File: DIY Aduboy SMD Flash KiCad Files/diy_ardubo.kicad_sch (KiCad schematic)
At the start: 21 parts, among them J1 Conn_02x01, J2 Conn_01x07_Pin, J3 Conn_02x03_Odd_Even, J4 Conn_01x01_Pin, Q1 BC557, SW1 SW_Push, SW2 SW_Push, SW3 SW_Push, SW4 SW_Push, SW5 SW_Push, SW6 SW_Push, SW7 SW_Push, SW8 SW_SPDT, U1 ProMicro, U2 W25Q128JVS

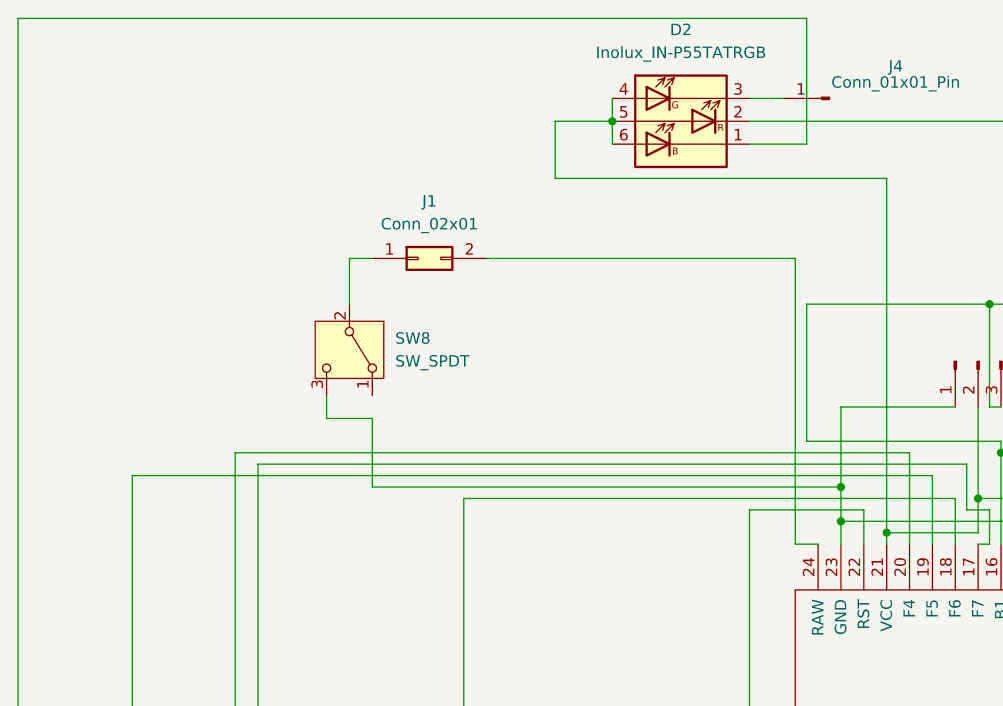
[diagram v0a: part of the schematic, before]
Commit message: Updated Schematics
Fixed ground pin issue with switch
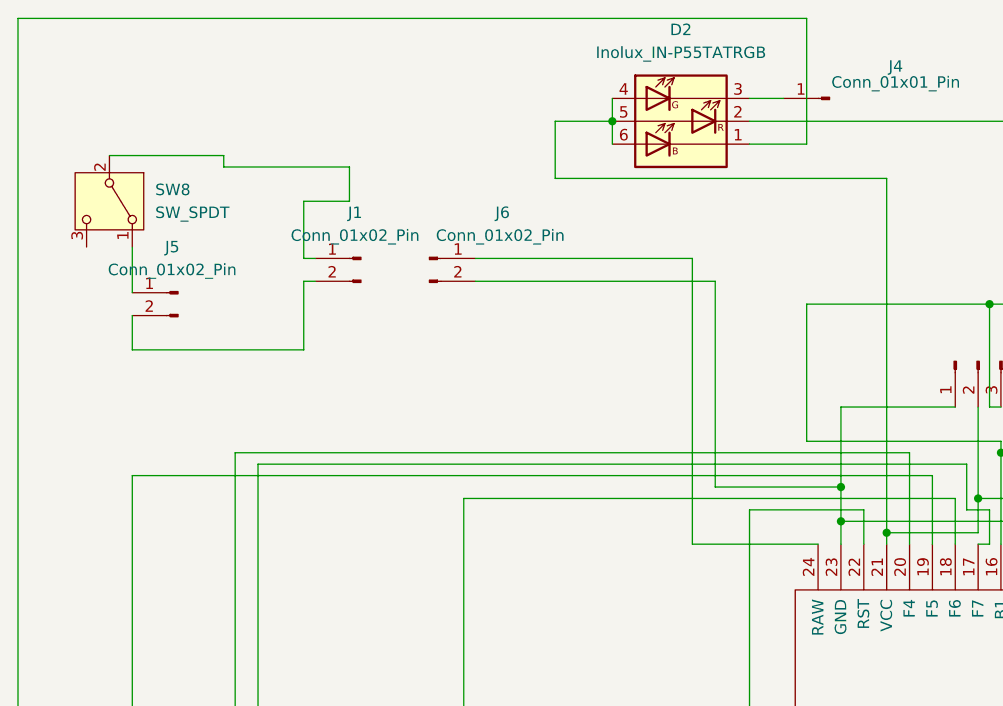
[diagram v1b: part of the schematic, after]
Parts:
- removed J1: Conn_02x01, Connector_PinHeader_2.54mm:PinHeader_2x01_P2.54mm_Vertical, symbol Connector_Generic:Conn_02x01
- added J1, J5, J6: Conn_01x02_Pin, Connector_PinHeader_2.54mm:PinHeader_1x02_P2.54mm_Vertical, symbol Connector:Conn_01x02_Pin
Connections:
- net at SW8.2 (B): now also J1.1 (Pin_1)
- net at U1.24 (RAW): now also J6.1 (Pin_1)
- net at C1.2, J2.1 (GND), R3.2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: now also J6.2 (Pin_2); no longer SW8.3 (C)
- net at SW8.1 (A): now also J5.1 (Pin_1)
- new net: J1.2 (Pin_2), J5.2 (Pin_2)
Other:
- moved on the sheet: SW8
